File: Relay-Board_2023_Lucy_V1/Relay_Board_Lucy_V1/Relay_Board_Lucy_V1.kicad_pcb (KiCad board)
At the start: 4 copper layers, 106.7 x 99.1 mm, 114 parts, among them J1 Battery Power, J2 VP0265540000G, J3 VP0265540000G, J4 VP0265540000G, J5 VP0265540000G, J6 SWD_HEADER, J7 USB_B_Micro, J8 Conn_02x14_Top_Bottom, J9 DE9_Receptacle_MountingHoles, K1 HE1AN-W-DC12V-Y6, K2 HE1AN-W-DC12V-Y6, K3 PTRH-1C-12S-1-X, K4 PTRH-1C-12S-1-X, Q1 SI2302A-TPMSCT-ND, Q2 SI2302A-TPMSCT-ND, Q3 SI2302A-TPMSCT-ND, Q4 SI2302A-TPMSCT-ND, Q5 SI2302A-TPMSCT-ND, SW1 PTS815 SJM 250 SMTR LFS, SW2 PTS815 SJM 250 SMTR LFS, U1 ACS770LCB-050U-PFF, U10 STM32F446RETx, U2 ACS770LCB-050U-PFF, U3 MAX14572, U4 TSV914IPT, U5 TSV914IPT, U6 ACS770LCB-050U-PFF, U7 LD39050PU33R, U9 MCP2542FD-E/SN, X1 OXETDLJANF-8MHZ

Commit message: Board layout is done and routed
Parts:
- removed D1: BLUE, LED_SMD:LED_0805_2012Metric
- removed H5: MountingHole_2.2mm_M2, MountingHole:MountingHole_2.2mm_M2
- D10, D11, D2: moved to F.Cu
- R1: value 10k -> 160
- SW2: footprint Inductor_SMD:L_1206_3216Metric -> Button_Switch_SMD:SW_SPST_PTS810
- TP1, TP2: footprint TestPoint:TestPoint_THTPad_D2.0mm_Drill1.0mm -> TestPoint:TestPoint_Pad_1.0x1.0mm
- moved D13 275.0 mm to (187.6, 105.0)
- moved R29 269.5 mm to (186.9, 110.5)
- moved R28 269.0 mm to (186.9, 112.0)
- moved Q3 265.7 mm to (187.4, 107.9), turned to 0 degrees
- moved U3 253.6 mm to (163.2, 124.5)
- moved R21 248.0 mm to (168.1, 138.4), turned to 90 degrees
- moved R22 245.9 mm to (166.6, 138.4), turned to -90 degrees
- moved Q4 245.1 mm to (106.6, 103.1), turned to -90 degrees
- moved TP1 244.0 mm to (156.7, 92.3)
- moved R23 243.8 mm to (165.1, 138.4), turned to 90 degrees
- moved R24 241.7 mm to (163.6, 138.4), turned to -90 degrees
- moved SW2 241.1 mm to (182.5, 120.4), turned to 90 degrees
- moved R3 240.8 mm to (170.3, 127.4), turned to 0 degrees
- moved R5 240.1 mm to (170.3, 129.0), turned to 0 degrees
- moved R2 239.8 mm to (169.5, 123.7), turned to 0 degrees
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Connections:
- net /MCU/PA11 renamed /MCU/USB_D-
- net /MCU/PA12 renamed /MCU/USB_D+
- C23 pad 1: +3.3VA -> +3V3
- D2 pad 1: unconnected-(D2-A1-Pad1) -> /TO_LED
- J8 pad 1: /MCU/PC0 -> /MCU/PA2
- J8 pad 10: /MCU/PC10 -> /MCU/PC13
- J8 pad 11: /MCU/PA1 -> /MCU/PB4
- J8 pad 12: /MCU/PC11 -> /MCU/PB5
- J8 pad 13: /MCU/PA2 -> /MCU/PD2
- J8 pad 14: /MCU/PC12 -> /MCU/PB3
- J8 pad 15: /MCU/PA3 -> /MCU/PC11
- J8 pad 16: /MCU/PD2 -> /MCU/PC12
- J8 pad 17: /MCU/PC13 -> /MCU/PA15
- J8 pad 18: /MCU/PA15 -> /MCU/PC10
- J8 pad 19: /MCU/PC14 -> /MCU/PC7
- J8 pad 2: /MCU/PB3 -> /MCU/PA1
- J8 pad 20: /MCU/PA9 -> /MCU/PC6
- J8 pad 21: /MCU/PC15 -> /MCU/PA9
- J8 pad 22: /MCU/PA10 -> /MCU/PC8
- J8 pad 23: /MCU/PC6 -> unconnected-(J8-Pin_23-Pad23)
- J8 pad 24: unconnected-(J8-Pin_24-Pad24) -> /MCU/PA10
- J8 pad 25: /MCU/PC7 -> unconnected-(J8-Pin_25-Pad25)
- J8 pad 27: /MCU/PC8 -> unconnected-(J8-Pin_27-Pad27)
- J8 pad 3: /MCU/PC1 -> /MCU/PC2
- J8 pad 4: /MCU/PB4 -> /MCU/PA0
- J8 pad 5: /MCU/PC2 -> /MCU/PC0
- J8 pad 6: /MCU/PB5 -> /MCU/PC1
- J8 pad 7: /MCU/PC3 -> /MCU/PC14
- J8 pad 8: /MCU/PB6 -> /MCU/PC15
- J8 pad 9: /MCU/PA0 -> /MCU/PB6
- JP1 pad 1: +5V -> UNPROTECTED_5V
- R1 pad 1: Net-(D1-A) -> /TO_LED
- R19 pad 2: /MOTOR+ -> /FC+
- R9 pad 2: /FC+ -> /MOTOR+
- U9 pad 5: +3.3VA -> +3V3
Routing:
- net UNPROTECTED_12V: track 0.00 -> 429.1 mm
- net +3V3: track 12.2 -> 233.0 mm, vias 0 -> 3
- net +5V: track 0.00 -> 206.8 mm
- net /MCU/PB0: track 0.00 -> 137.0 mm, vias 0 -> 10
- net /MCU/PA1: track 2.78 -> 123.9 mm, vias 0 -> 1
- net UNPROTECTED_5V: track 0.00 -> 120.8 mm, vias 0 -> 1
- net /MCU/PC1: track 0.00 -> 120.1 mm, vias 0 -> 1
- net /MCU/PA2: track 2.43 -> 122.0 mm, vias 0 -> 1
- net /MCU/PA0: track 3.53 -> 122.6 mm, vias 0 -> 1
- net /MCU/PC15: track 0.00 -> 118.1 mm, vias 0 -> 1
- net /MCU/PB15: track 4.25 -> 121.9 mm, vias 0 -> 2
- net /MCU/PC2: track 0.00 -> 117.3 mm, vias 0 -> 1
- net /MCU/PB14: track 4.25 -> 120.5 mm, vias 0 -> 2
- net /MCU/PC0: track 0.00 -> 116.2 mm, vias 0 -> 1
- net /MCU/PC13: track 0.00 -> 116.0 mm, vias 0 -> 1
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- added copper zone on In2.Cu, net GNDA
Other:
- board text added: "+"
- board text added: "5V_OK"
- board text added: "CANBus"
- board text added: "CAP - +"
- board text added: "FC -+"
- board text added: "MTR + -"
- board text added: "MTR CAP"
- board text added: "RES + -"
- board text added: "RES DCHG"
- board text added: "SWD"
- board text added: "S_{CLK}"
- board text added: "S_{DIO}"
- board text added: "⏚"

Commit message: $
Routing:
- net /MCU/PB12: track 117.1 -> 112.4 mm

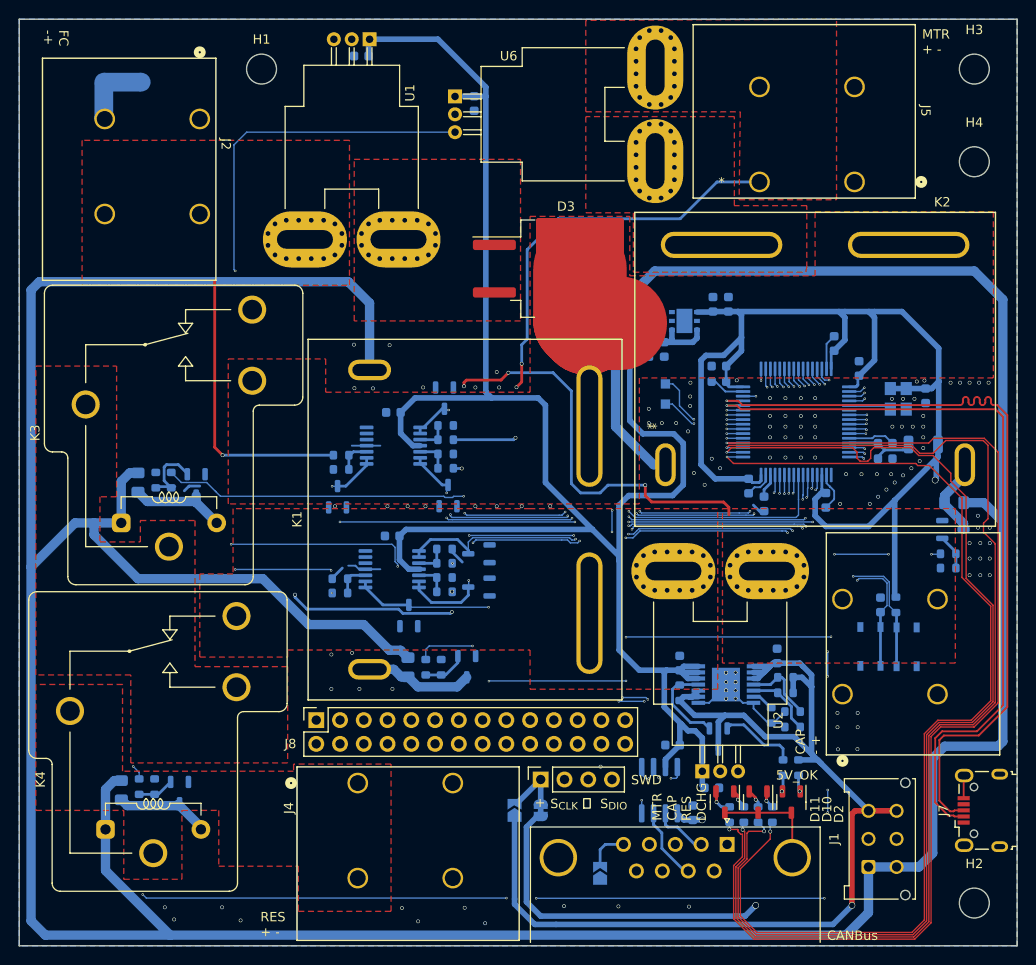
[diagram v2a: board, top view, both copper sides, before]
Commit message: Finished the relay board. Once gerbers and drill files are generated we can order from jlc
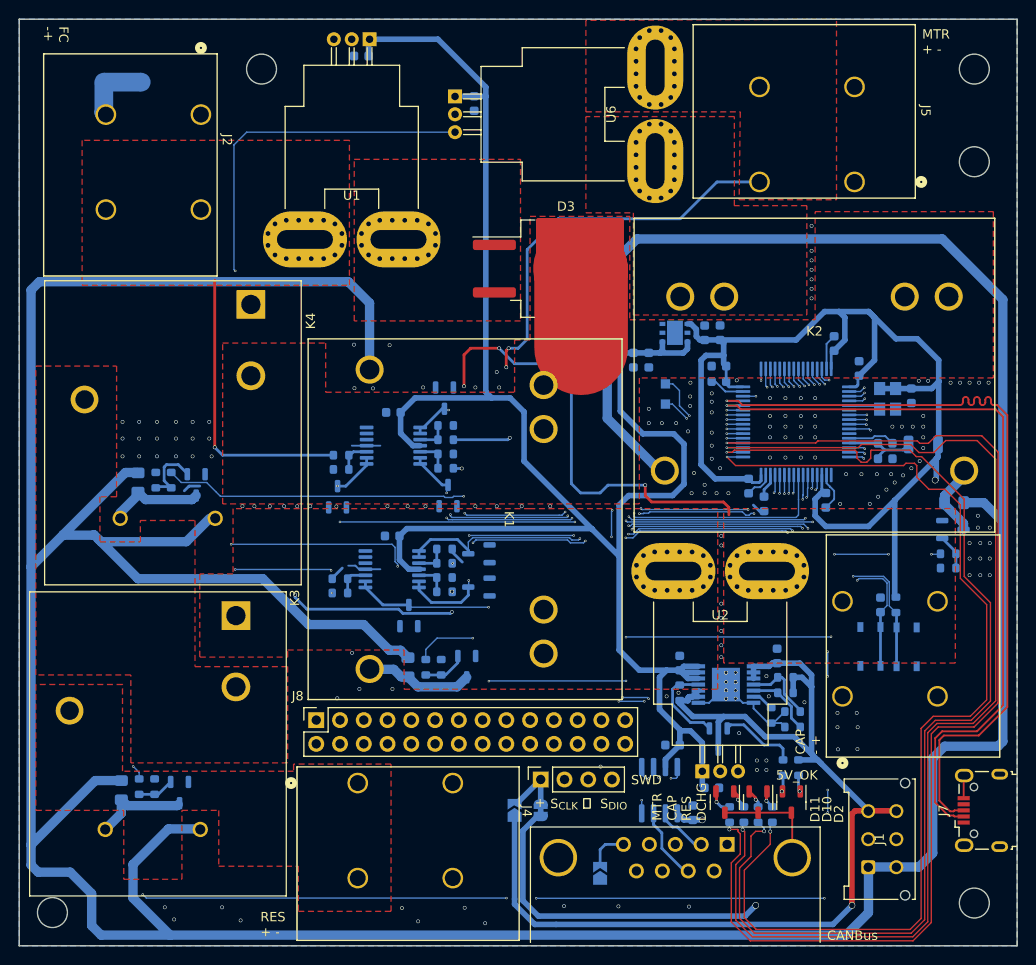
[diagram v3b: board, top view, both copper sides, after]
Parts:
- added H2: MountingHole, MountingHole:MountingHole_3.2mm_M3, F.Cu at (91.2, 148.8)
- J1: value Battery Power -> STD_PWR_HEADER; footprint Connector_Molex:Molex_Micro-Fit_3.0_43045-0612_2x03_P3.00mm_Vertical -> RB_FTP:STD_PWR_HEADER
- K1, K2: footprint RB_FTP:HE1AN-W-DC12V-Y6 -> RB_FTP:HE1AN-P-DC12V-H18
- K3, K4: value PTRH-1C-12S-1-X -> T9AV5L12-12; footprint RB_FTP:PTRH-1C-12S-1-X -> RB_FTP:T9AV5L12-12
- moved K4 59.6 mm to (112.4, 83.8), turned to 0 degrees
- moved K2 15.1 mm to (172.7, 88.9)
- moved K1 14.7 mm to (137.8, 106.8)
- moved K3 10.3 mm to (110.8, 117.1), turned to 0 degrees
- moved J1 3.41 mm to (180.1, 141.0)
- moved C14 3.18 mm to (160.9, 86.9)
- moved C16 3.16 mm to (162.6, 86.9)
- moved C10 2.01 mm to (154.9, 89.8)
- moved C8 2.01 mm to (153.3, 89.8)
- moved U7 1.63 mm to (157.7, 86.9)
- moved C9 1.52 mm to (183.0, 93.6)
- moved X1 1.14 mm to (180.5, 93.9)
- moved J2 0.48 mm to (107.1, 63.5)
- moved J3 0.23 mm to (175.6, 125.7)
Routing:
- net UNPROTECTED_12V: track 429.1 -> 456.4 mm
- net /CAP+: track 52.9 -> 57.8 mm
- net /MCU/PC2: track 117.3 -> 121.3 mm
- net /MCU/PA1: track 123.9 -> 127.8 mm
- net /MCU/PB4: track 106.5 -> 110.2 mm
- net /MCU/PB5: track 112.2 -> 116.0 mm
- net /MCU/PB6: track 108.2 -> 111.9 mm
- net /MCU/PB3: track 110.1 -> 113.9 mm
- net /MCU/PC13: track 116.0 -> 119.8 mm
- net /MCU/PC14: track 113.3 -> 117.1 mm
- net /MCU/PC0: track 116.2 -> 119.9 mm
- net /MCU/PA0: track 122.6 -> 126.4 mm
- net /MCU/PA2: track 122.0 -> 125.8 mm
- net /MCU/PC1: track 120.1 -> 123.8 mm
- net +5V: track 206.8 -> 203.5 mm
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
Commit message: $
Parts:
- removed the H2 at (91.2, 148.8)
- added G***: LOGO, RB_FTP:ecocar_logo, B.Cu at (145.9, 77.0)
- added J10: STD_PWR_HEADER, RB_FTP:STD_PWR_HEADER, F.Cu at (94.6, 76.3)
- added R34: 120, Resistor_SMD:R_0603_1608Metric, F.Cu at (156.0, 138.2)
- U2: value ACS770LCB-050U-PFF -> ACS770LCB-050B-PFF
- moved H4 127.1 mm to (91.2, 148.8)
- moved H1 22.4 mm to (91.2, 56.9)
- moved NT1 14.6 mm to (113.0, 57.1)
- moved J2 8.16 mm to (111.1, 70.6), turned to 180 degrees
- moved U1 2.16 mm to (127.2, 55.5)
- moved H3 2.05 mm to (190.8, 56.9)
- moved C1 2.03 mm to (126.2, 57.3)
- moved H2 1.44 mm to (190.8, 148.8)
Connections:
- net /CAP Discharge Relay/NORMALLY_CLOSED renamed /TO_CAPS
- J4 pad 3: GNDPWR -> /RES-
- J4 pad 4: GNDPWR -> /RES-
- J8 pad 25: unconnected-(J8-Pin_25-Pad25) -> GNDA
- J8 pad 26: unconnected-(J8-Pin_26-Pad26) -> UNPROTECTED_12V
- J8 pad 27: unconnected-(J8-Pin_27-Pad27) -> GNDA
- J8 pad 28: unconnected-(J8-Pin_28-Pad28) -> UNPROTECTED_12V
- K3 pad 2: /CAP Discharge Relay/NORMALLY_OPEN -> GNDPWR
- K3 pad 5: /RES+ -> /RES-
- K4 pad 1: /RES Relay/NORMALLY_CLOSED -> GNDPWR
- K4 pad 5: /CAP Discharge Relay/NORMALLY_OPEN -> /RES+
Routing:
- net UNPROTECTED_12V: track 456.4 -> 488.5 mm
- net /MCU/CAN_H: track 7.93 -> 10.9 mm, vias 0 -> 1
- net /MCU/CAN_L: track 5.61 -> 8.52 mm, vias 0 -> 1
- net +5V: track 203.5 -> 201.4 mm
- net GNDA: track 59.2 -> 61.2 mm, vias 175 -> 177
- net /MOTOR_CURR: track 82.6 -> 83.6 mm
- net /MCU/PB14: track 120.0 -> 121.0 mm
- net /CAP_CURR: track 91.5 -> 92.5 mm
- net /FC_CURR: track 88.3 -> 89.1 mm
- net /MCU/PA4: track 64.8 -> 65.5 mm
- net /MCU/PB15: track 122.6 -> 123.2 mm
- net /MCU/PB13: track 115.8 -> 115.2 mm
- added copper zone on F.Cu, net /RES-
- removed copper zone on F.Cu, net /CAP Discharge Relay/NORMALLY_OPEN
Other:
- board text added: "${COMMENT1} Issued: ${ISSUE_DATE}"
- board text added: "${TITLE} - ${REVISION}"

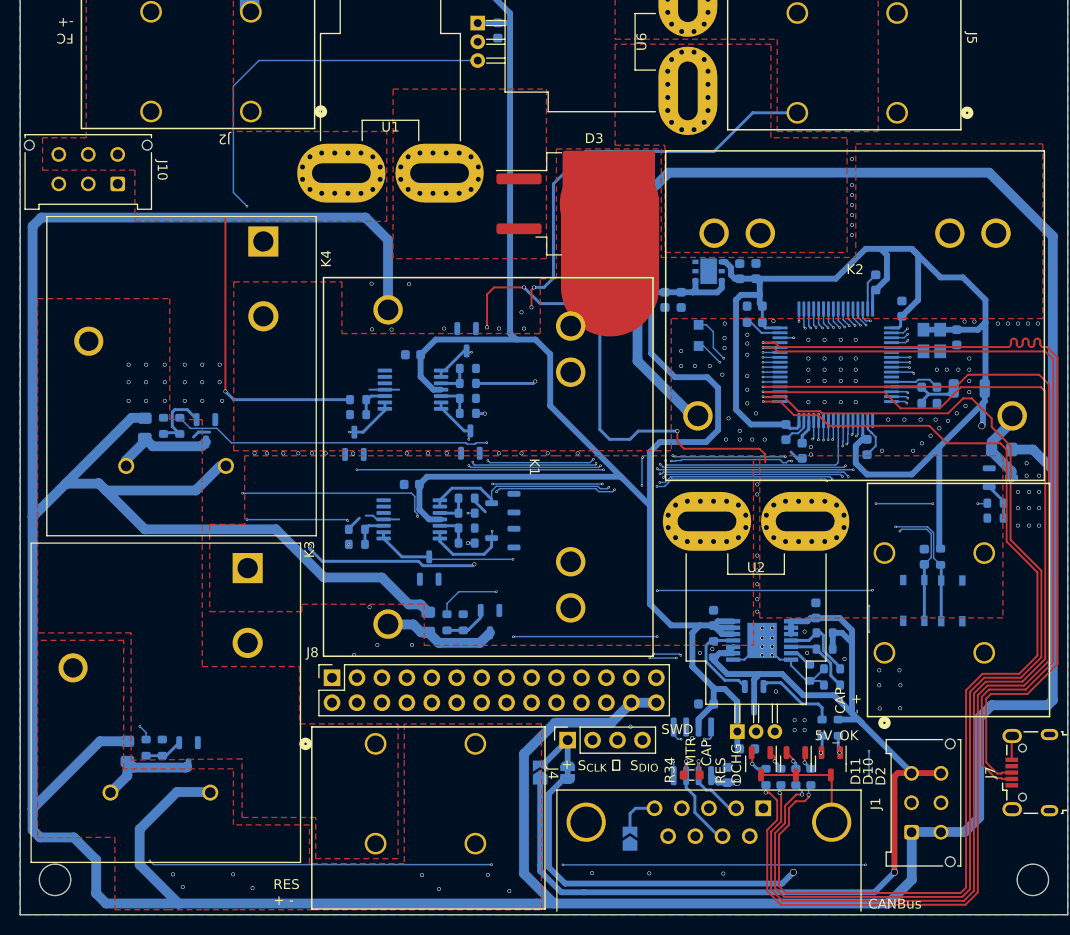
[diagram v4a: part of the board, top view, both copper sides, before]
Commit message: Started work on the BOM file and I updated the lower current relays to work with 50A models
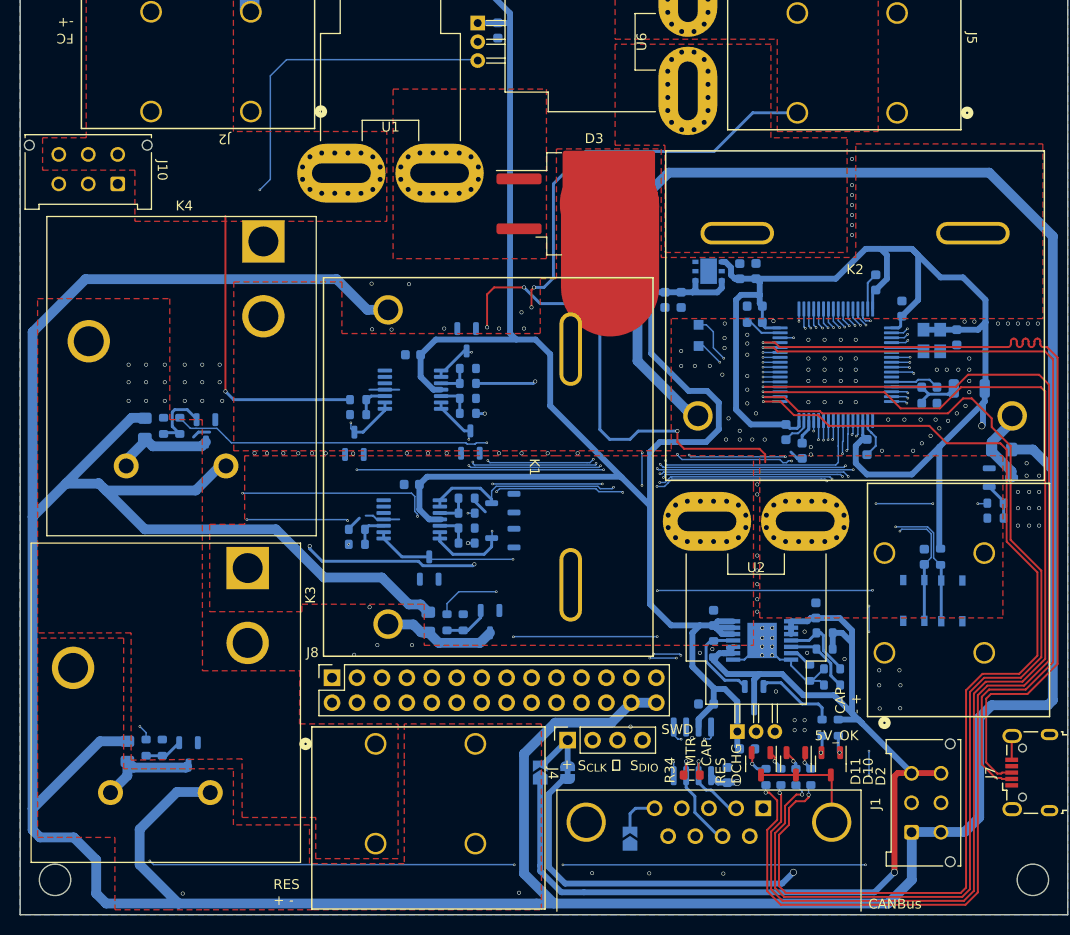
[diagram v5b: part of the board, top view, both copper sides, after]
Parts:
- K1, K2: value HE1AN-W-DC12V-Y6 -> HE1AN-P-DC12V-Y5; footprint RB_FTP:HE1AN-P-DC12V-H18 -> RB_FTP:HE1AN-P-DC12V-Y5
- K3, K4: value T9AV5L12-12 -> J115F11CH12VDCS61.5; footprint RB_FTP:T9AV5L12-12 -> RB_FTP:J115F11CH12VDCS61.5
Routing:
- net UNPROTECTED_12V: track 488.5 -> 472.8 mm
- net /MOTOR_CURR: track 83.6 -> 81.6 mm
- net /MCU/PA4: track 65.5 -> 67.0 mm
- net /MCU/PB10: track 26.5 -> 25.2 mm
- net /MCU/PA13: track 61.2 -> 60.1 mm
- net /MCU/PB1: track 79.4 -> 80.4 mm
- net /MCU/PB0: track 137.0 -> 136.1 mm
- net /FC_CURR: track 89.1 -> 89.9 mm
- net +5V: track 201.4 -> 200.6 mm
- net /MCU/PA7: track 57.2 -> 56.6 mm
- net GNDA: vias 177 -> 171

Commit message: updated, created gerbers, created p&p, created BOM's
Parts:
- J7: footprint Connector_USB:USB_Micro-B_Wuerth_629105150521 -> RB_FTP:USB_Micro-B_Wuerth_629105150521
